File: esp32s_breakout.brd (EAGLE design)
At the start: 51.9 x 36.8 mm, 15 parts, among them IC1 AMS1117, J1 PJ-007

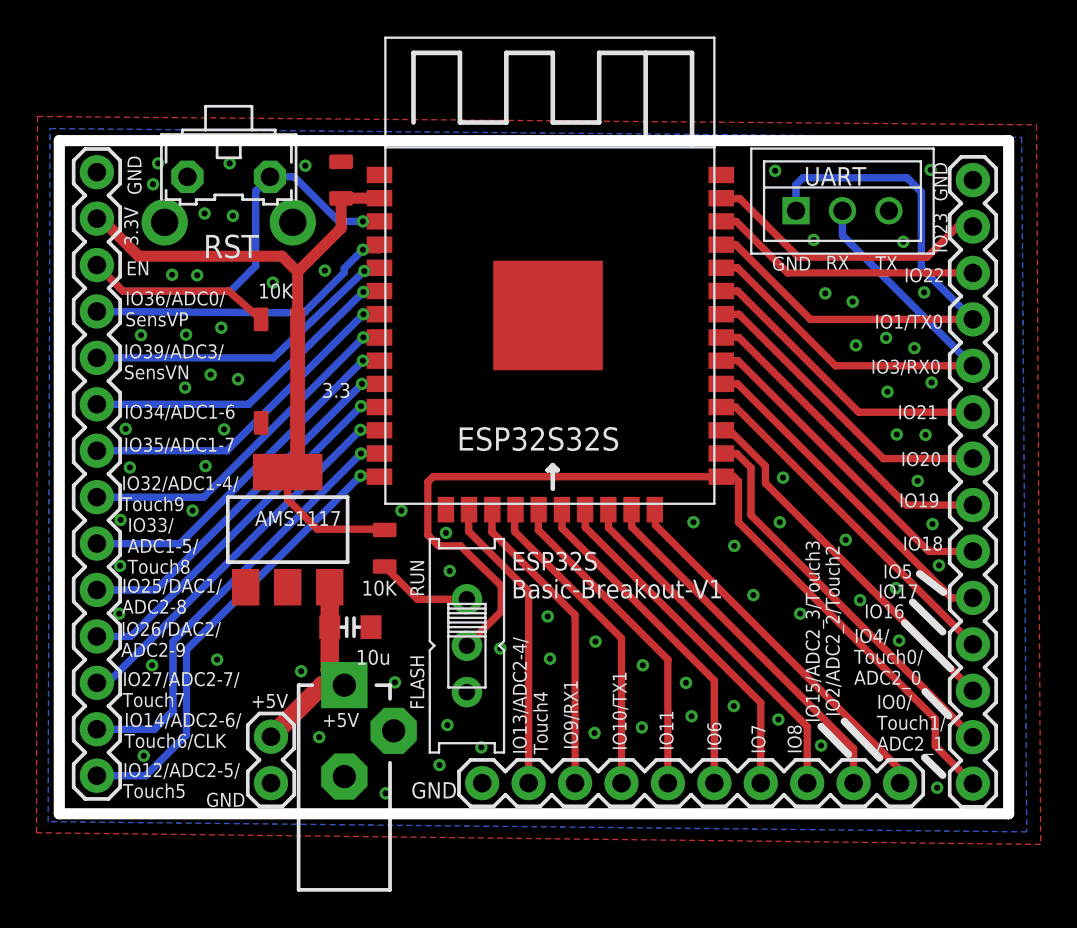
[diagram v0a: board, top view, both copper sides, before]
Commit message: squeeze to get under 5cm
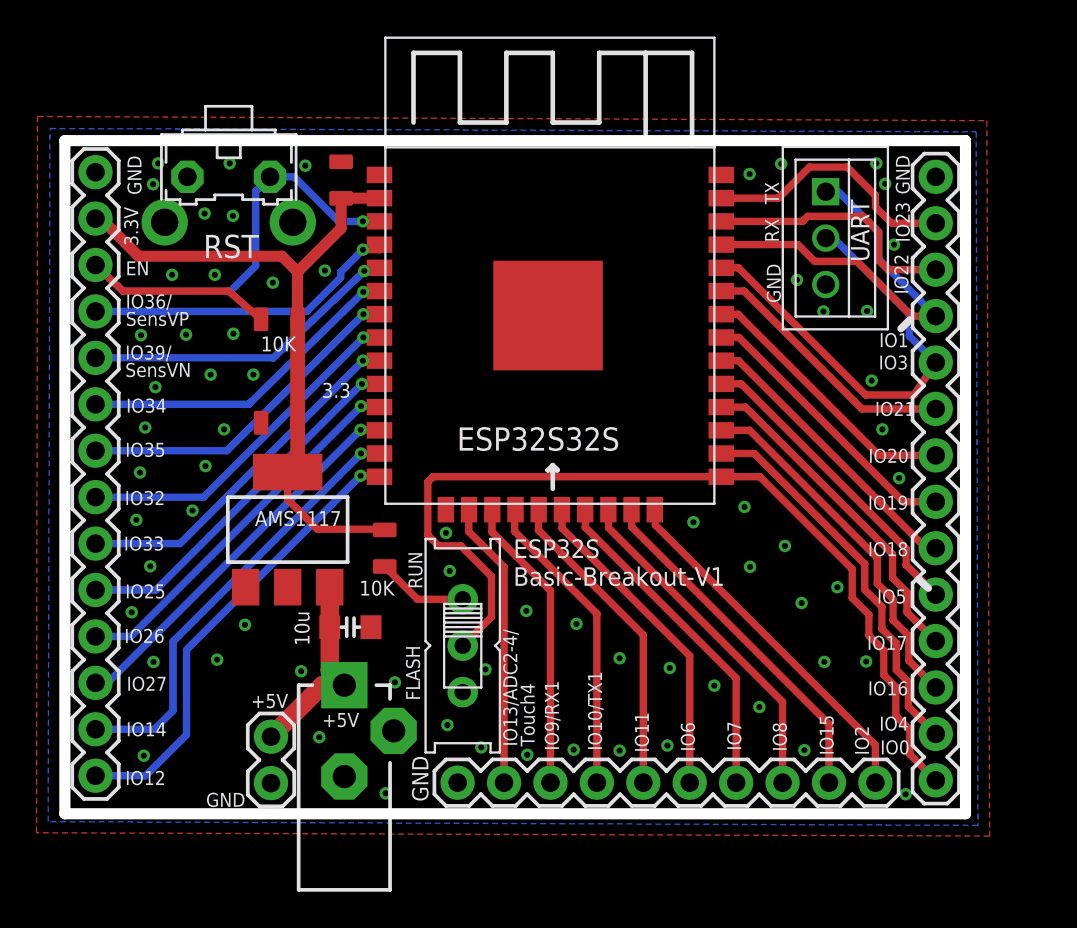
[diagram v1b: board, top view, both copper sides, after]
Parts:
- moved JP2 2.04 mm to (53.7, 41.6)
- moved UART 1.76 mm to (47.7, 38.2), turned to 270 degrees
- moved JP3 1.35 mm to (27.6, 8.43)
- moved SPDT 0.23 mm to (27.9, 15.9)
- moved JP1 0.08 mm to (7.77, 41.8)
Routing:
- net ETX: track 32.4 -> 23.1 mm
- net ERX: track 27.4 -> 25.1 mm
- net IO19: track 17.6 -> 15.5 mm
- net IO18: track 18.1 -> 16.0 mm
- net IO20: track 17.0 -> 14.9 mm
- net IO21: track 16.5 -> 14.4 mm
- net IO23: track 15.8 -> 14.1 mm
- net IO5: track 18.6 -> 17.0 mm
- net IO22: track 14.9 -> 14.0 mm
- net IO17: track 19.1 -> 18.4 mm
- net IO11: track 17.9 -> 17.3 mm
- net IO10: track 17.4 -> 16.8 mm
- net IO7: track 18.9 -> 18.4 mm
- net IO13: track 16.3 -> 15.7 mm
- net IO9: track 16.9 -> 16.3 mm
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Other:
- board size 51.9 x 36.8 mm -> 49.3 x 36.8 mm
- board text added: "IO0"
- board text added: "IO1"
- board text added: "IO12"
- board text added: "IO14"
- board text added: "IO15"
- board text added: "IO2"
- board text added: "IO25"
- board text added: "IO26"
- board text added: "IO27"
- board text added: "IO3"
- board text added: "IO32"
- board text added: "IO33"
- board text added: "IO34"
- board text added: "IO35"
- board text added: "IO36/ SensVP"
- board text added: "IO39/ SensVN"
- board text added: "IO4"
- board text removed: "IO0/ Touch1/ ADC2_1"
- board text removed: "IO1/TX0"
- board text removed: "IO12/ADC2-5/ Touch5"
- board text removed: "IO14/ADC2-6/ Touch6/CLK"
- board text removed: "IO15/ADC2_3/Touch3"
- board text removed: "IO2/ADC2_2/Touch2"
- board text removed: "IO25/DAC1/ ADC2-8"
- board text removed: "IO26/DAC2/ ADC2-9"
- board text removed: "IO27/ADC2-7/ Touch7"
- board text removed: "IO3/RX0"
- board text removed: "IO32/ADC1-4/ Touch9"
- board text removed: "IO33/ ADC1-5/ Touch8"
- board text removed: "IO34/ADC1-6"
- board text removed: "IO35/ADC1-7"
- board text removed: "IO36/ADC0/ SensVP"
- board text removed: "IO39/ADC3/ SensVN"
- board text removed: "IO4/ Touch0/ ADC2_0"
